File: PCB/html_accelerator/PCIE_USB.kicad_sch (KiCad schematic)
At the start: 1 part, among them U1 MCS9990

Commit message: schematic updates
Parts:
- added C28: Cin, symbol Device:C
- added C28: 470pF, symbol Device:C
- added C33: 10uF, symbol Device:C_Polarized_US
- added C33: Cout, symbol Device:C_Polarized_US
- added D1: zz, symbol Device:D_Zener_Filled
- added L1: L, symbol Device:L
- added R20: 1.2k, symbol Device:R_US
- added R20 (x4): 12k, symbol Device:R_US
- added R20: rsc, symbol Device:R_US
- added R20 (x4): 10k, symbol Device:R_US
- added R20: 3.6k, symbol Device:R_US
- added U11: AP1513, html_accel_footprints:SOP-8L_DIO, symbol html_accel_Symbols:AP1513SG-13
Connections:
- net at U1.102 (USB1_OVCI_N): now also R20.2
- net at U1.116 (USB2_IBERF): now also R20.1
- net at U1.122 (USB2_OVCI_N): now also R20.2
- net at U1.125 (USB3_OVCI_N): now also R20.2
- net at U1.57 (USB3_IBREF): now also R20.1
- net at U1.89 (USB0_IBREF): now also R20.1
- net at U1.96 (USB1_IBREF): now also R20.1
- net at U1.99 (USB0_OVCI_N): now also R20.2
- new net: R20.1, R20.2
- new net: D1.1 (K), L1.1
- new net +12V: C28.1, R20.1
- new net +3V3: C33.1, L1.2, R20.1, R20.1, R20.1, R20.1, R20.1
- new net GND: C28.2, C28.2, C33.2, C33.2, D1.2 (A), R20.2, R20.2, R20.2, R20.2, R20.2
- no-connect marks 0 -> 6
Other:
- note added: "todo: Wire up AP1513"
- title: (none) -> USB, 5v POWER

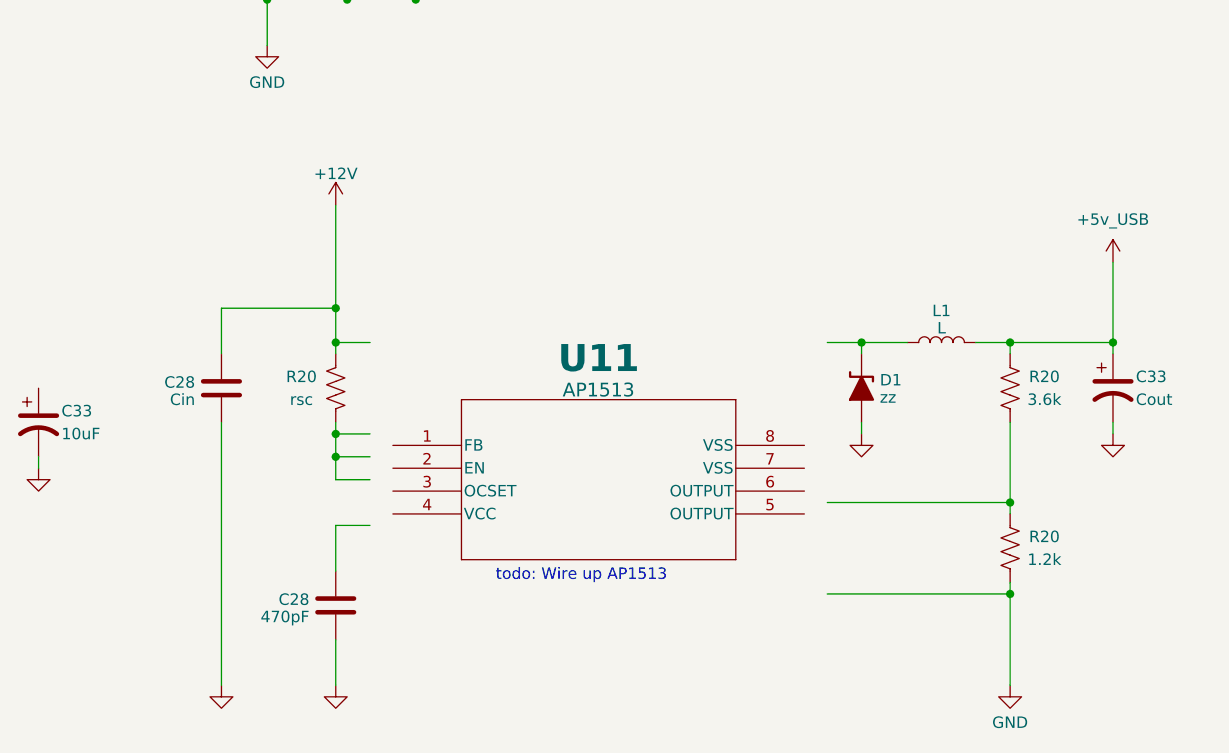
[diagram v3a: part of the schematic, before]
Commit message: Voltage regulator and footprints
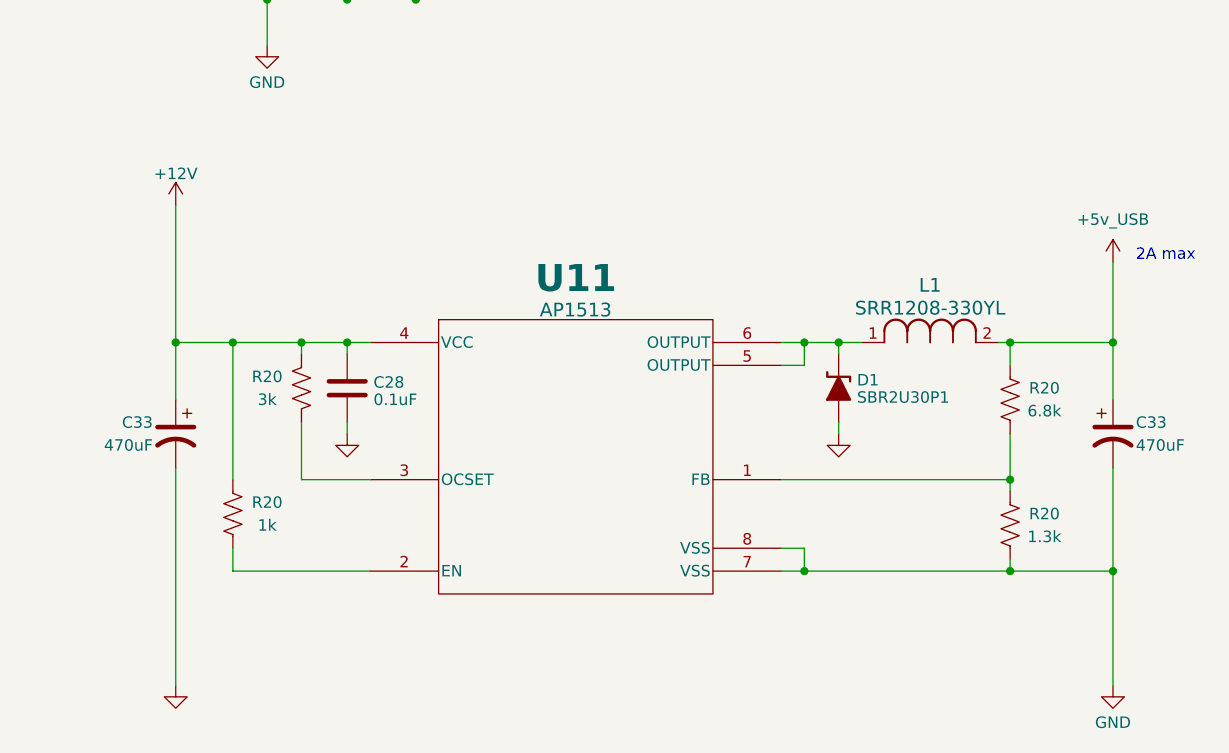
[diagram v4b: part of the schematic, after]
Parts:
- removed C28: Cin, symbol Device:C
- removed C28: 470pF, symbol Device:C
- removed L1: L, symbol Device:L
- added C28: 0.1uF, symbol Device:C
- added L1: SRR1208-330YL, html_accel_footprints:IND_BOURNS_SRR1208, symbol html_accel_Symbols:SRR1208-330YL
- added R20: 1k, symbol Device:R_US
- C33: value 10uF -> 470uF
- C33: value Cout -> 470uF
- D1: value zz -> SBR2U30P1; footprint (none) -> html_accel_footprints:DIODE_SBR3M30P1_1P78X2P8_DIO-M
- R20: value 1.2k -> 1.3k
- R20: value rsc -> 3k
- R20: value 3.6k -> 6.8k
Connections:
- net +12V: now also C33.1, U11.4 (VCC), C28.1, R20.1
- net +3V3: now also L1.2
- net GND: now also U11.7 (VSS), U11.8 (VSS), C28.2
- net at R20.1, R20.2: now also U11.1 (FB)
- net at R20.2: now also U11.3 (OCSET)
- net at U11.2 (EN): now also R20.2
- net at U11.5 (OUTPUT): now also D1.1 (K), U11.6 (OUTPUT), L1.1
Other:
- note added: "2A max"
- note removed: "todo: Wire up AP1513"
- moved on the sheet: C33, D1, R20

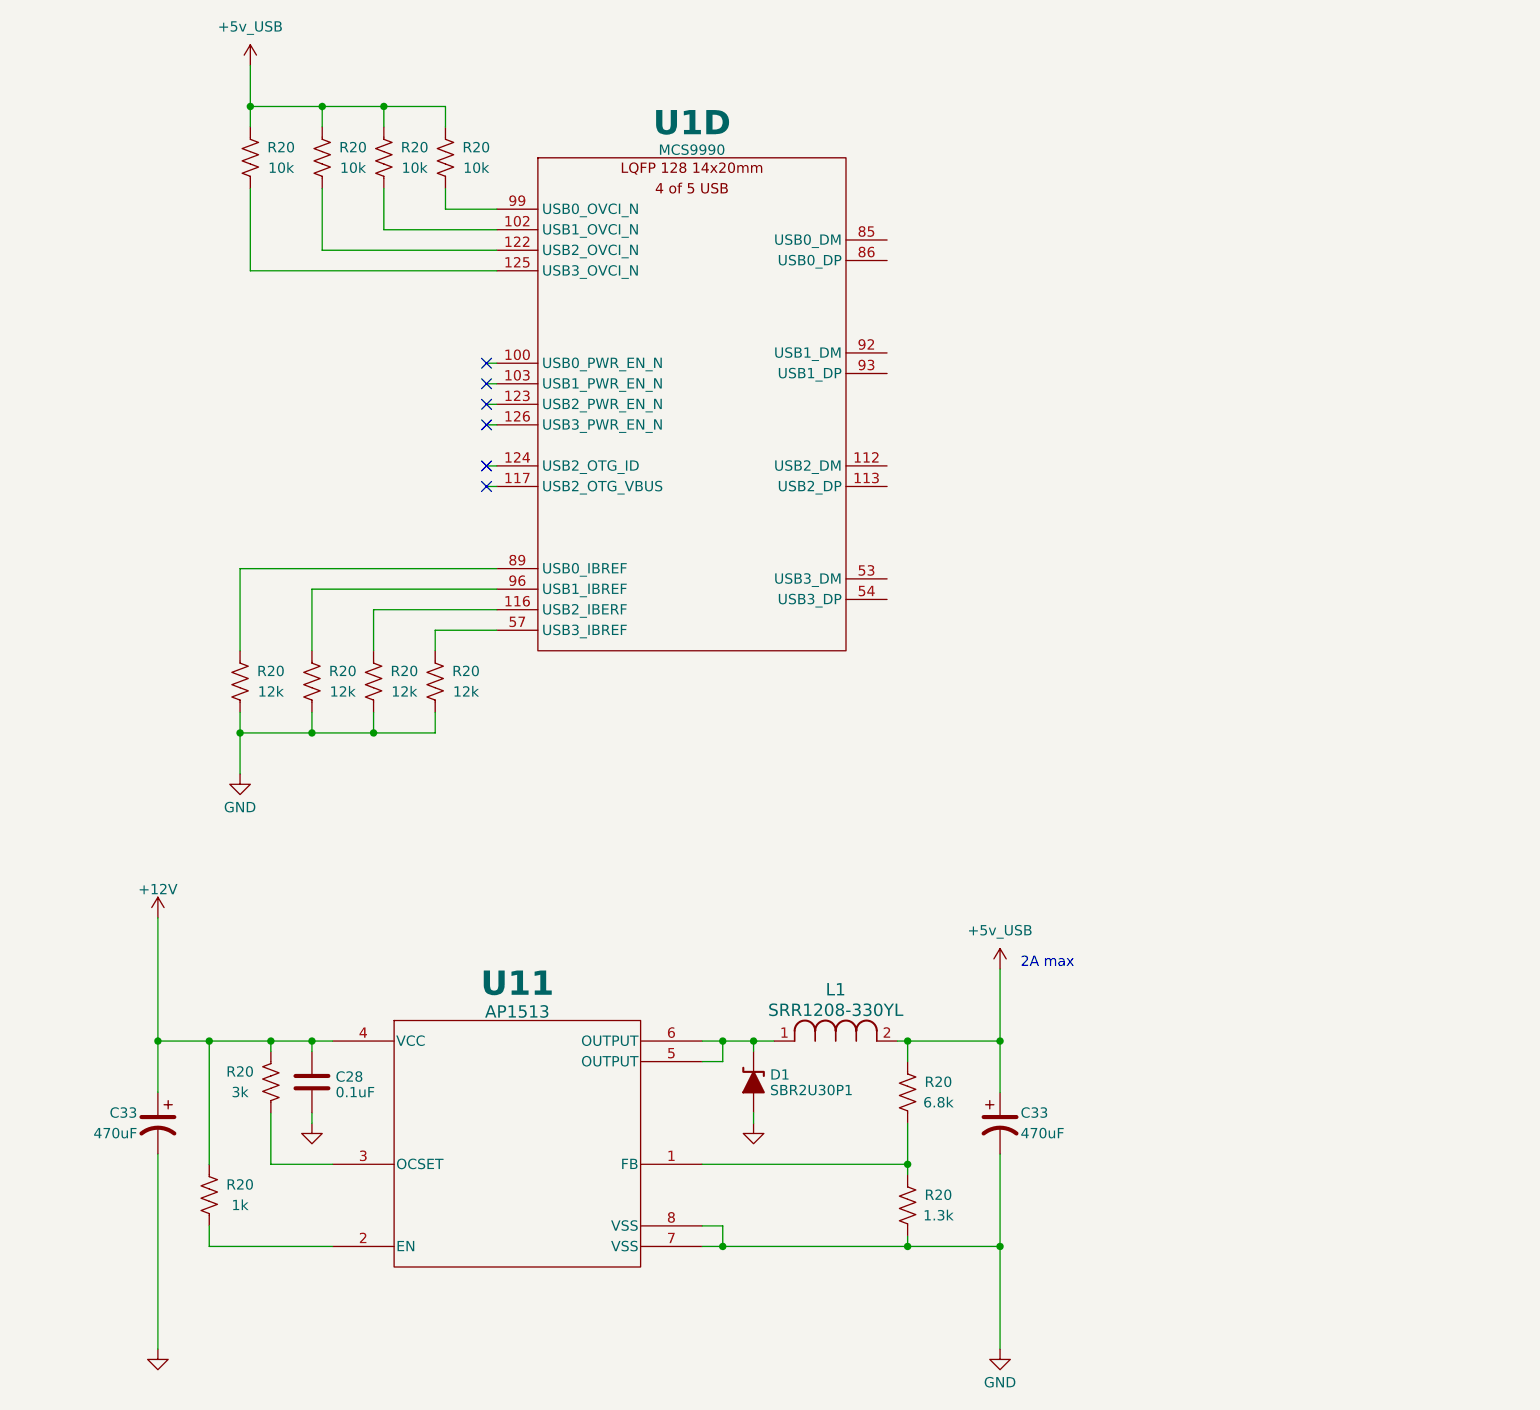
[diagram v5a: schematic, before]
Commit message: EMMC symbols and netlist
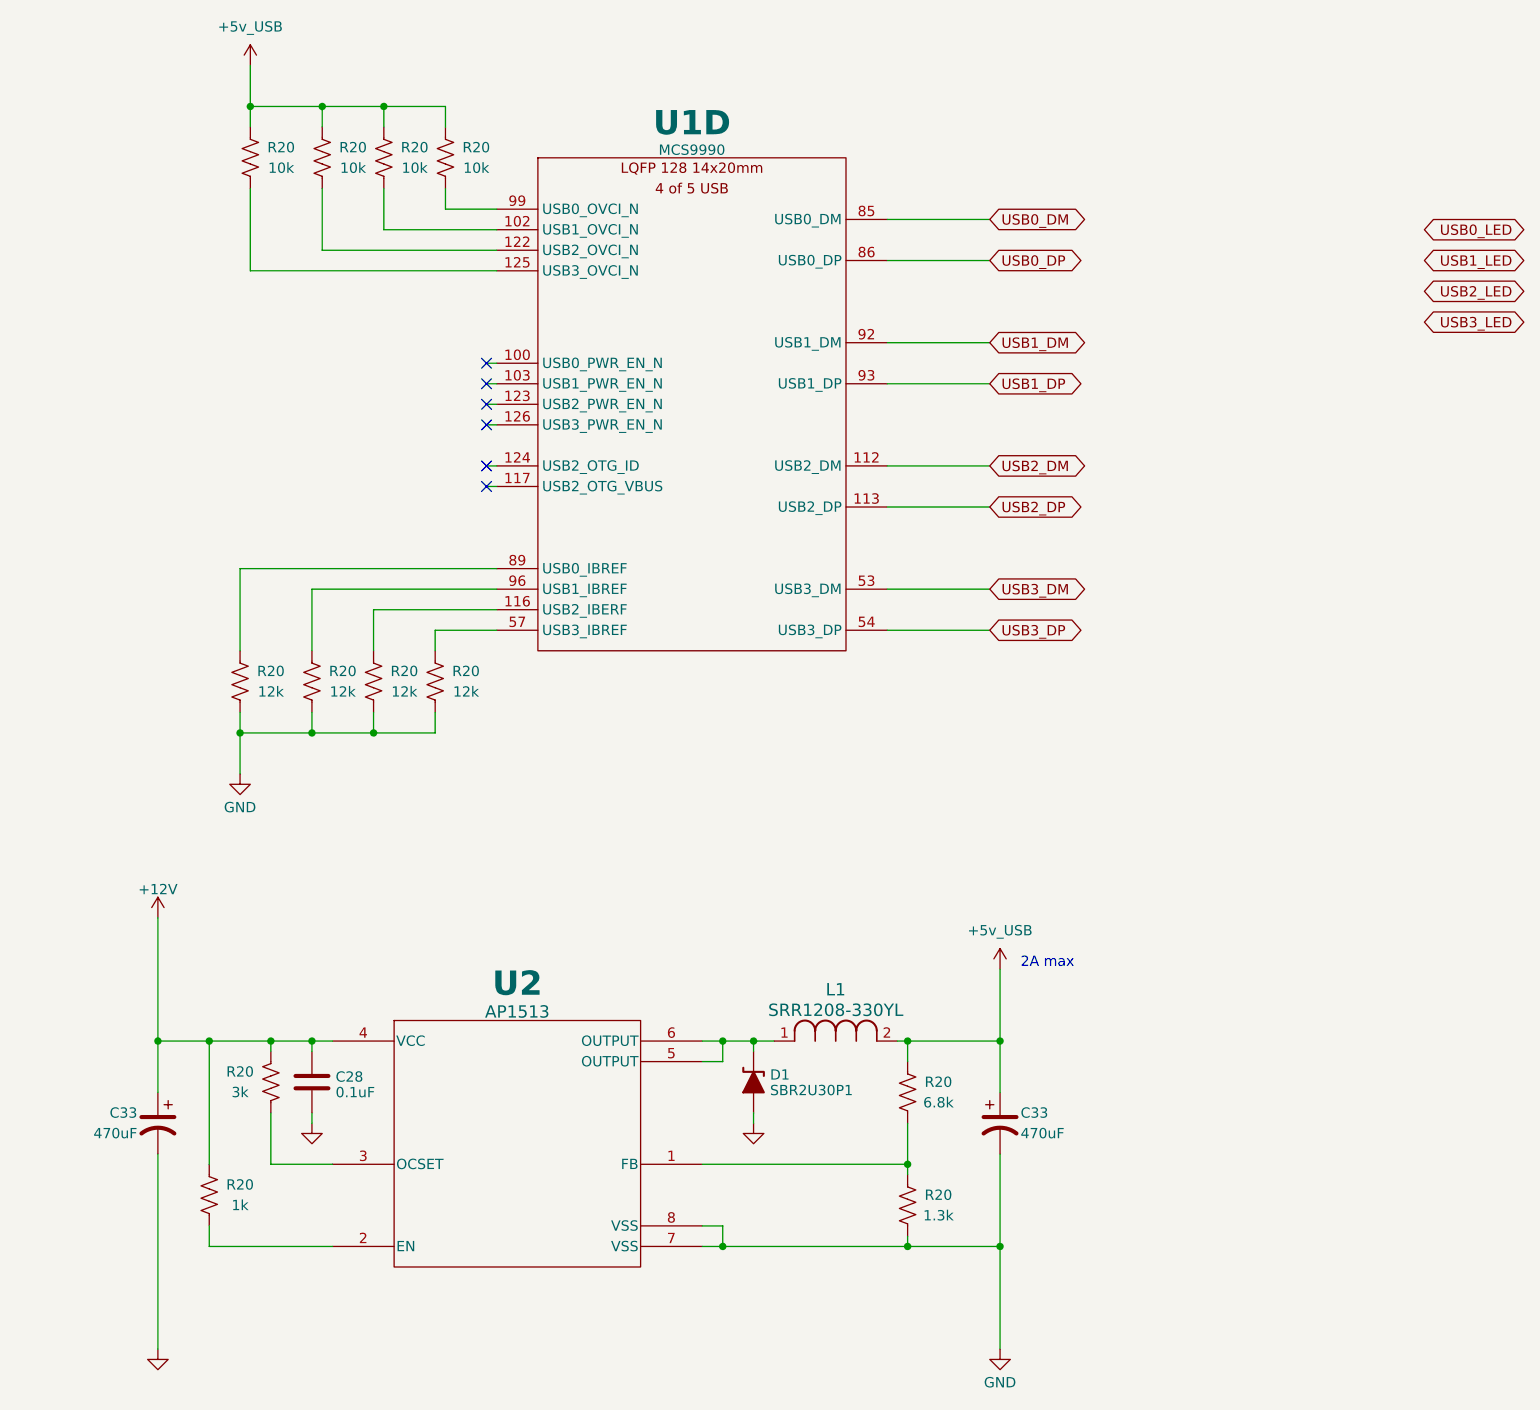
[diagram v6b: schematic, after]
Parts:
- renumbered U11 to U2
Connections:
- net USB2_DM: now reaches U1.112 (USB2_DM)
- net USB2_DP: now reaches U1.113 (USB2_DP)
- net USB3_DM: now reaches U1.53 (USB3_DM)
- net USB3_DP: now reaches U1.54 (USB3_DP)
- net USB0_DM: now reaches U1.85 (USB0_DM)
- net USB0_DP: now reaches U1.86 (USB0_DP)
- net USB1_DM: now reaches U1.92 (USB1_DM)
- net USB1_DP: now reaches U1.93 (USB1_DP)
